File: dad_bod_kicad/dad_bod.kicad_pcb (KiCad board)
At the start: 2 copper layers, 98.5 x 69.9 mm, 135 parts, among them J1 Conn_01x01, J10 Conn_01x03_Male, J11 BNC5-J-P-GN-RA-BH2D, J12 USB4085-GF-A_REVA4, J13 Conn_01x03_Male, J2 Conn_01x01, J3 Conn_01x01, J4 Conn_01x01, J5 Conn_01x03_Male, J6 Conn_02x15_Odd_Even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

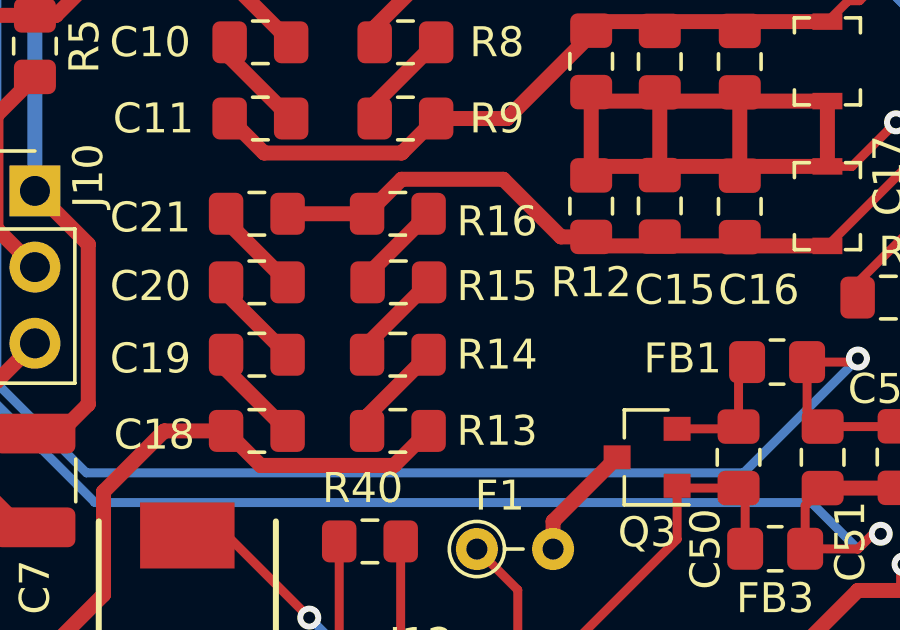
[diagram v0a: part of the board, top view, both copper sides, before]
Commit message: Added beach_bod_01; Initial layout complete
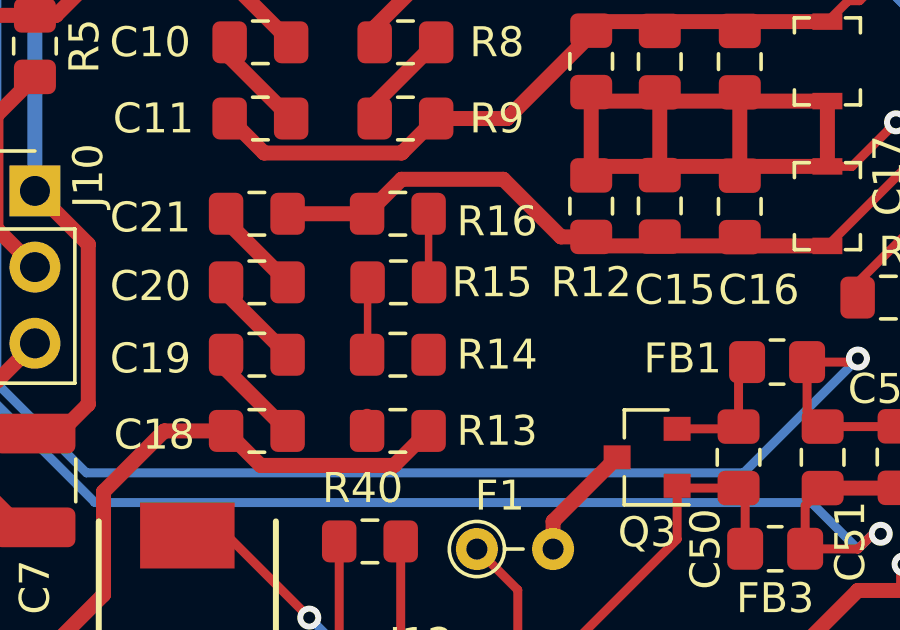
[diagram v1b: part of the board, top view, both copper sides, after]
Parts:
- turned R15 to 180 degrees
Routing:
- net Net-(R13-Pad1): track 3.39 -> 0.49 mm
- net Net-(R15-Pad1): track 2.87 -> 2.29 mm
- net Net-(R14-Pad1): track 2.92 -> 2.42 mm
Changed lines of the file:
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@@
   )
   (footprint "Resistor_SMD:R_0805_2012Metric_Pad1.15x1.40mm_HandSolder" (layer "F.Cu")
-    (at 80.948 109.982)
+    (at 80.948 109.982 180)
     (descr "Resistor SMD 0805 (2012 Metric), square (rectangular) end terminal, IPC_7351 nominal with elongated pad for handsoldering. (Body size source: https://docs.google.com/spreadsheets/d/1BsfQQcO9C6DZCsRaXUlFlo91Tg2WpOkGARC1WS5S8t0/edit?usp=sharing), generated with kicad-footprint-generator")
     (tags "resistor handsolder")
@@
     (property "Sheetname" "")
     (attr smd)
-    (fp_text reference "R15" (at 3.293 0.127) (layer "F.SilkS")
+    (fp_text reference "R15" (at -3.126 0) (layer "F.SilkS")
       (effects (font (size 1 1) (thickness 0.15)))
     )
@@
     (fp_line (start -1 0.6) (end -1 -0.6) (layer "F.Fab") (width 0.1))
     (fp_line (start 1 -0.6) (end 1 0.6) (layer "F.Fab") (width 0.1))
-    (pad "1" smd roundrect locked (at -1.025 0) (size 1.15 1.4) (layers "F.Cu" "F.Paste" "F.Mask") (roundrect_rratio 0.2173913043)
+    (pad "1" smd roundrect locked (at -1.025 0 180) (size 1.15 1.4) (layers "F.Cu" "F.Paste" "F.Mask") (roundrect_rratio 0.2173913043)
       (net 72 "Net-(R15-Pad1)") (pintype "passive"))
-    (pad "2" smd roundrect locked (at 1.025 0) (size 1.15 1.4) (layers "F.Cu" "F.Paste" "F.Mask") (roundrect_rratio 0.2173913043)
+    (pad "2" smd roundrect locked (at 1.025 0 180) (size 1.15 1.4) (layers "F.Cu" "F.Paste" "F.Mask") (roundrect_rratio 0.2173913043)
       (net 71 "Net-(R14-Pad1)") (pintype "passive"))
     (model "${KISYS3DMOD}/Resistor_SMD.3dshapes/R_0805_2012Metric.wrl"
@@
   (segment (start 80.159 104.521) (end 80.159 104.031) (width 0.5) (layer "F.Cu") (net 69))
   (segment (start 80.159 104.031) (end 82.209 101.981) (width 0.5) (layer "F.Cu") (net 69))
-  (segment (start 79.905 114.445) (end 81.955 112.395) (width 0.5) (layer "F.Cu") (net 70))
   (segment (start 79.905 114.935) (end 79.905 114.445) (width 0.5) (layer "F.Cu") (net 70))
-  (segment (start 79.905 112.05) (end 81.973 109.982) (width 0.5) (layer "F.Cu") (net 71))
-  (segment (start 79.923 109.728) (end 81.955 107.696) (width 0.5) (layer "F.Cu") (net 72))
+  (segment (start 79.923 109.982) (end 79.923 112.377) (width 0.25) (layer "F.Cu") (net 71))
+  (segment (start 79.923 112.377) (end 79.905 112.395) (width 0.25) (layer "F.Cu") (net 71))
+  (segment (start 81.955 109.964) (end 81.973 109.982) (width 0.25) (layer "F.Cu") (net 72))
+  (segment (start 81.955 107.696) (end 81.955 109.964) (width 0.25) (layer "F.Cu") (net 72))
   (segment (start 110.6005 102.465478) (end 110.340042 102.20502) (width 0.3) (layer "F.Cu") (net 73))
   (segment (start 110.340042 102.20502) (end 109.06302 102.20502) (width 0.3) (layer "F.Cu") (net 73))
